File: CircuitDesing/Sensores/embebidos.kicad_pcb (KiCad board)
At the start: 2 copper layers, 45 parts, among them J1 Conn_01x03_Male, J2 Conn_01x02, Q1 BSS138, Q2 BSS138, Q3 BSS138, U1 ESP32-WROOM-32, U2 AMS1117-3.3

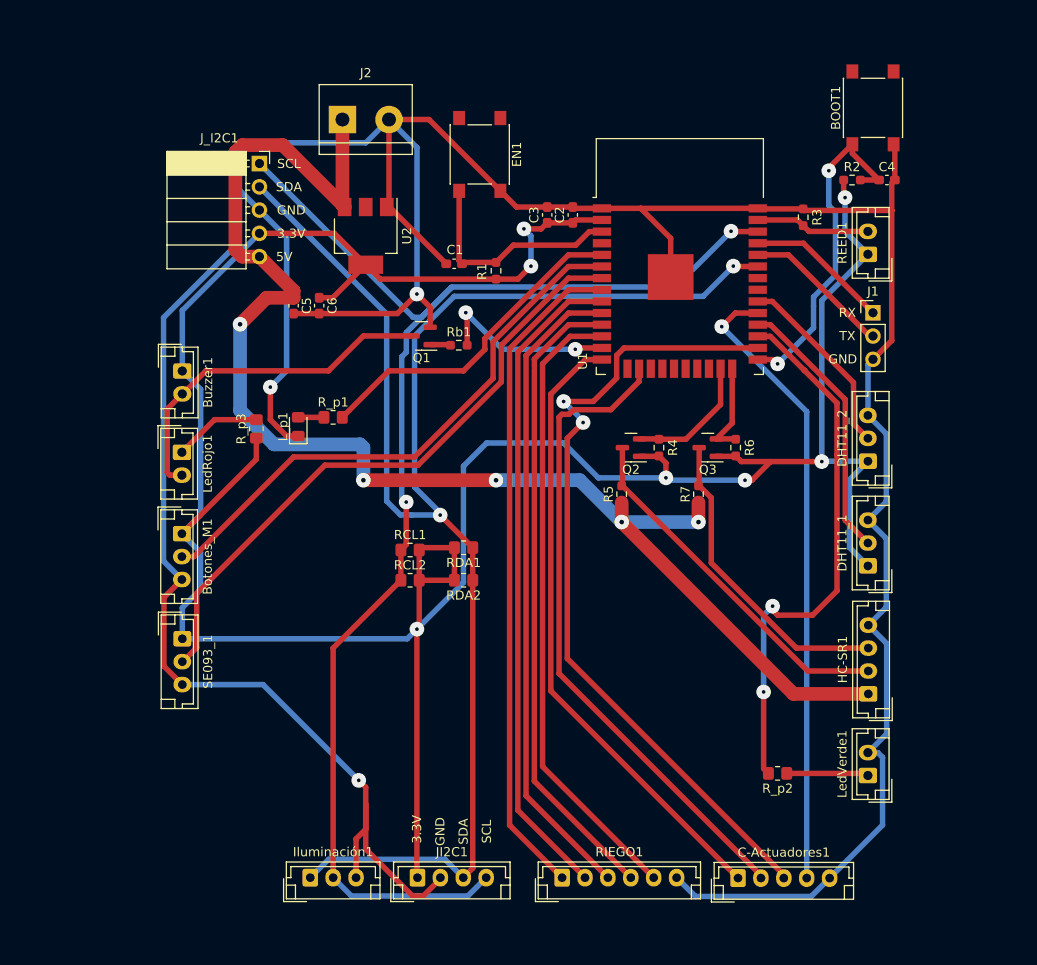
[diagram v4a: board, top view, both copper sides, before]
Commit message: Ruteo plano de tierra
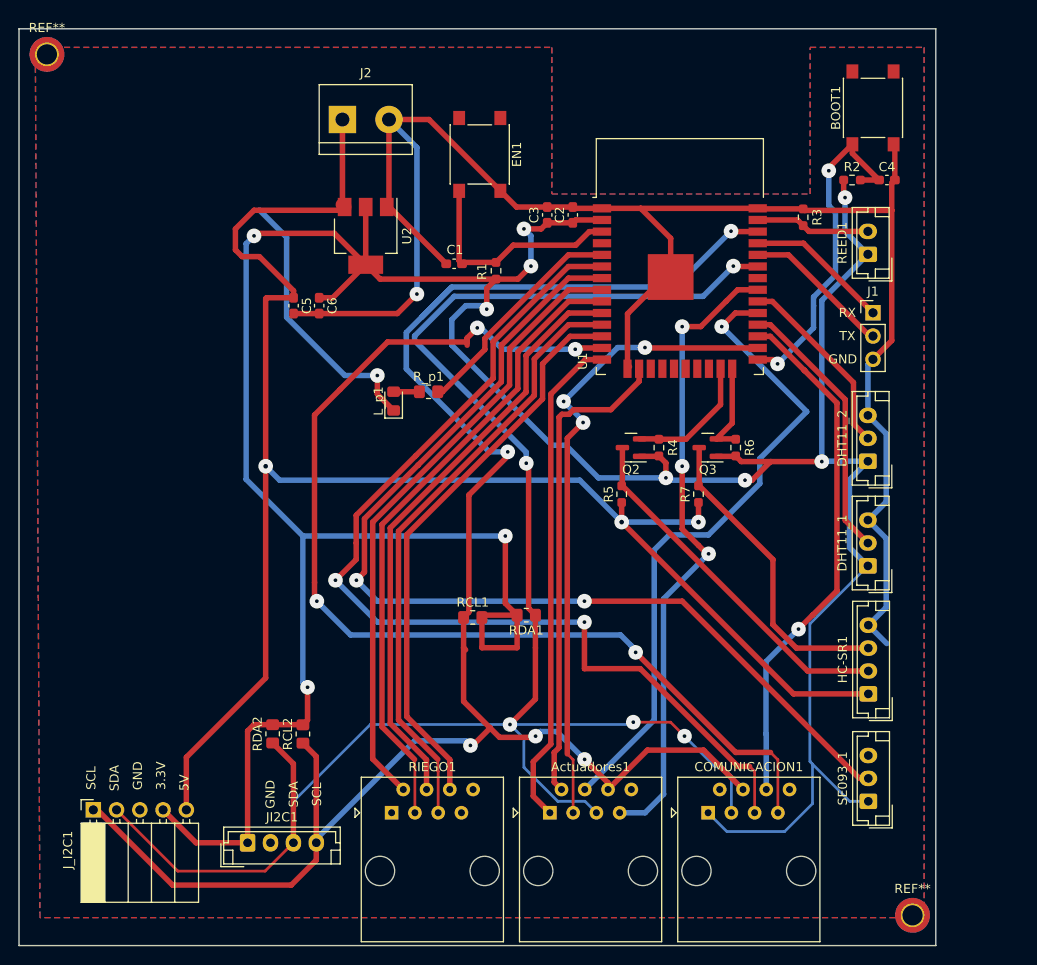
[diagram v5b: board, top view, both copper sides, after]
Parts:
- removed Botones_M1, Iluminación1: Conn_01x03, Connector_JST:JST_EH_B3B-EH-A_1x03_P2.50mm_Vertical
- removed Buzzer1, LedRojo1, LedVerde1: Conn_01x02, Connector_JST:JST_EH_B2B-EH-A_1x02_P2.50mm_Vertical
- removed C-Actuadores1: Conn_01x05, Connector_JST:JST_EH_B5B-EH-A_1x05_P2.50mm_Vertical
- removed Q1: BSS138, Package_TO_SOT_SMD:SOT-23
- removed R_p2: 47, Resistor_SMD:R_0805_2012Metric_Pad1.20x1.40mm_HandSolder
- removed R_p3: 1k, Resistor_SMD:R_0805_2012Metric_Pad1.20x1.40mm_HandSolder
- removed Rb1: 1k, Resistor_SMD:R_0603_1608Metric_Pad0.98x0.95mm_HandSolder
- added Actuadores1: RJ45, Connector_RJ:RJ45_Amphenol_54602-x08_Horizontal, F.Cu at (109.0, 149.3)
- added COMUNICACION1: RJ45, Connector_RJ:RJ45_Amphenol_54602-x08_Horizontal, F.Cu at (126.3, 149.3)
- added REF**: MountingHole_2.2mm_M2_ISO14580_Pad_TopBottom, MountingHole:MountingHole_2.2mm_M2_ISO14580_Pad_TopBottom, F.Cu at (148.6, 160.5)
- added REF**: MountingHole_2.2mm_M2_ISO14580_Pad_TopBottom, MountingHole:MountingHole_2.2mm_M2_ISO14580_Pad_TopBottom, F.Cu at (54.1, 66.5)
- RIEGO1: value Conn_01x06 -> RJ45; footprint Connector_JST:JST_EH_B6B-EH-A_1x06_P2.50mm_Vertical -> Connector_RJ:RJ45_Amphenol_54602-x08_Horizontal
- moved SE093_1 77.0 mm to (143.8, 148.1), turned to 90 degrees
- moved J_I2C1 72.8 mm to (59.2, 149.0), turned to 90 degrees
- moved RDA2 26.7 mm to (78.7, 140.7), turned to 90 degrees
- moved RCL2 20.5 mm to (82.0, 140.7), turned to 90 degrees
- moved RIEGO1 19.9 mm to (91.7, 149.3)
- moved JI2C1 18.9 mm to (76.0, 152.6)
- moved R_p1 10.8 mm to (95.8, 103.4)
- moved L_p1 10.8 mm to (91.9, 104.4)
- moved RDA1 10.1 mm to (106.4, 127.8)
- moved RCL1 10.1 mm to (100.6, 128.0)
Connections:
- RIEGO1 pad 1: /ControlV5 -> GND
- RIEGO1 pad 2: /ControlV4 -> /ControlV5
- RIEGO1 pad 3: /ControlV3 -> /ControlV4
- RIEGO1 pad 4: /ConrolV2 -> /ControlV3
- RIEGO1 pad 5: /ControlV1 -> /ConrolV2
- RIEGO1 pad 6: GND -> /ControlV1
- U1 pad 31: /Esp32Schematic/IO19 -> /Adicional
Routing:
- net GND: track 399.6 -> 223.8 mm, vias 3 -> 2
- net /Buzzer: track 20.2 -> 120.8 mm, vias 2 -> 4
- net /Adicional: track 0.00 -> 69.9 mm, vias 0 -> 3
- net /Botones: track 61.3 -> 110.3 mm, vias 0 -> 2
- net SCL: track 153.8 -> 201.9 mm, vias 2 -> 5
- net 3.3v: track 316.0 -> 362.7 mm, vias 7 -> 10
- net /lm393_1_D: track 69.0 -> 111.1 mm, vias 0 -> 2
- net Net-(Buzzer1-Pad2): track 38.8 -> 0.00 mm
- net SDA: track 167.7 -> 202.9 mm, vias 2 -> 5
- net 5v: track 156.9 -> 185.0 mm, vias 5 -> 3
- net /C_temp1: track 71.2 -> 52.9 mm
- net /C_temp2: track 88.5 -> 70.4 mm, vias 2 -> 3
- net /C_ilum: track 68.4 -> 54.4 mm
- net /LedU1: track 36.4 -> 24.8 mm
- net Net-(LedRojo1-Pad1): track 9.60 -> 0.00 mm
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- added copper zone on B.Cu, net GND
- added copper zone on F.Cu, net GND
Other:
- board outline added: 100.1 x 100.1 mm

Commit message: Programacion
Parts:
- removed REF** (x2): MountingHole_2.2mm_M2_ISO14580_Pad_TopBottom, MountingHole:MountingHole_2.2mm_M2_ISO14580_Pad_TopBottom
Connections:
- COMUNICACION1 pad 8: unconnected-(COMUNICACION1-Pad8) -> GND
- RIEGO1 pad 7: unconnected-(RIEGO1-Pad7) -> 5v
- RIEGO1 pad 8: unconnected-(RIEGO1-Pad8) -> GND
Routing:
- net GND: track 223.8 -> 180.1 mm, vias 2 -> 4
- net 5v: track 185.0 -> 224.2 mm
- net Net-(C1-Pad2): track 24.8 -> 32.8 mm
- net /Esp32Schematic/BOOT: track 37.4 -> 45.4 mm
- net SCL: track 201.9 -> 197.2 mm
- net /C_hum: track 71.4 -> 67.2 mm
- net /C_temp2: track 70.4 -> 71.5 mm, vias 3 -> 2
- net /Adicional: track 69.9 -> 69.0 mm
- net /Buzzer: track 120.8 -> 120.2 mm
- net /Led_Verde: track 57.3 -> 56.7 mm
